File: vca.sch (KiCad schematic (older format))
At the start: 26 parts, among them Q1* 2N3904, Q2* 2N3904, Q3 2N3904, U3 TL072

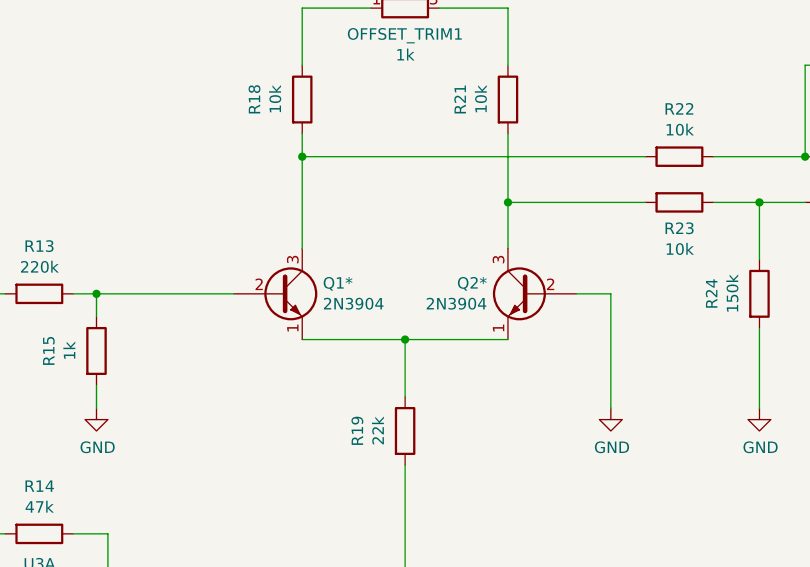
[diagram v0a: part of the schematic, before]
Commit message: Fix envelope trigger
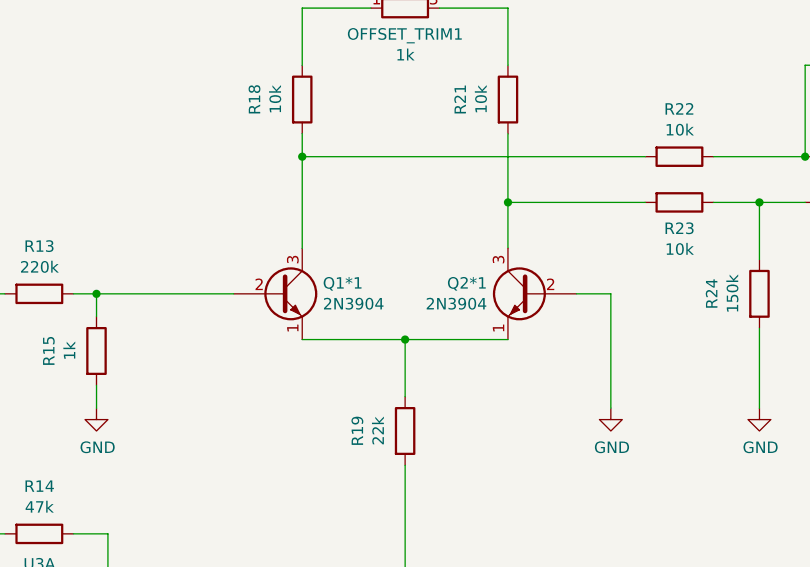
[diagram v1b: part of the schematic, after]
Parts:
- renumbered Q1* to Q1*1, Q2* to Q2*1
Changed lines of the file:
@@
 Title "VCA"
 Date "2021-02-15"
-Rev "v1.0.0"
+Rev "v1.0.1"
 Comp "Jan Knipper"
 Comment1 "github.com/polykit/vca-adsr"
@@
 $EndComp
 $Comp
-L Transistor_BJT:2N3904 Q2*
+L Transistor_BJT:2N3904 Q2*1
 U 1 1 604C170B
 P 6250 3600
-F 0 "Q2*" H 6441 3646 50  0000 L CNN
+F 0 "Q2*1" H 6441 3646 50  0000 L CNN
 F 1 "2N3904" H 6441 3555 50  0000 L CNN
 F 2 "Package_TO_SOT_THT:TO-92_Inline_Wide" H 6450 3525 50  0001 L CIN
@@
 $EndComp
 $Comp
-L Transistor_BJT:2N3904 Q1*
+L Transistor_BJT:2N3904 Q1*1
 U 1 1 604C108A
 P 5150 3600
-F 0 "Q1*" H 5340 3646 50  0000 L CNN
+F 0 "Q1*1" H 5340 3646 50  0000 L CNN
 F 1 "2N3904" H 5340 3555 50  0000 L CNN
 F 2 "Package_TO_SOT_THT:TO-92_Inline_Wide" H 5350 3525 50  0001 L CIN
@@
 	5450 4850 5700 4850
 $Comp
-L power:+12V #PWR?
+L power:+12V #PWR0134
 U 1 1 604A0FB2
 P 8300 4600
-F 0 "#PWR?" H 8300 4450 50  0001 C CNN
+F 0 "#PWR0134" H 8300 4450 50  0001 C CNN
 F 1 "+12V" H 8315 4773 50  0000 C CNN
 F 2 "" H 8300 4600 50  0001 C CNN
@@
 Connection ~ 8300 4700
 $Comp
-L power:-12V #PWR?
+L power:-12V #PWR0135
 U 1 1 604ADCA8
 P 8300 5400
-F 0 "#PWR?" H 8300 5500 50  0001 C CNN
+F 0 "#PWR0135" H 8300 5500 50  0001 C CNN
 F 1 "-12V" H 8315 5573 50  0000 C CNN
 F 2 "" H 8300 5400 50  0001 C CNN
